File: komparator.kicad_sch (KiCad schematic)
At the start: 11 parts, among them Q1 2N3904, Q2 2N3904, Q3 2N3906

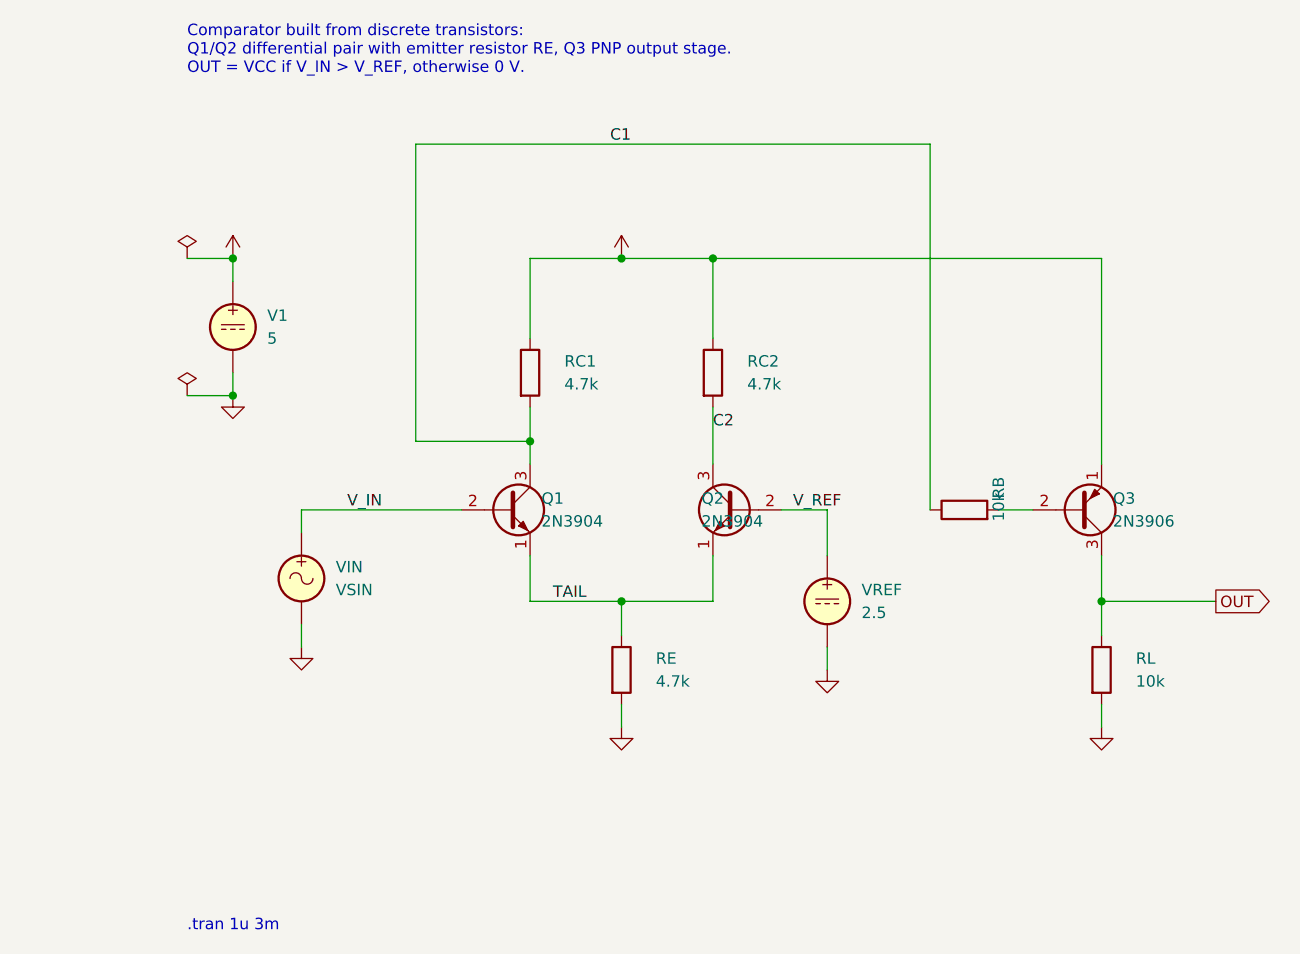
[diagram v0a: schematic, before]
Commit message: Run simulation with uv and take the KiCad schematic as parameter
- pyproject.toml + uv.lock replace requirements.txt
- simulate.py exports the given .kicad_sch via kicad-cli and simulates that
  netlist; VCC, V_REF and RE are read from the schematic
- schematic re-arranged by hand, references re-annotated by KiCad
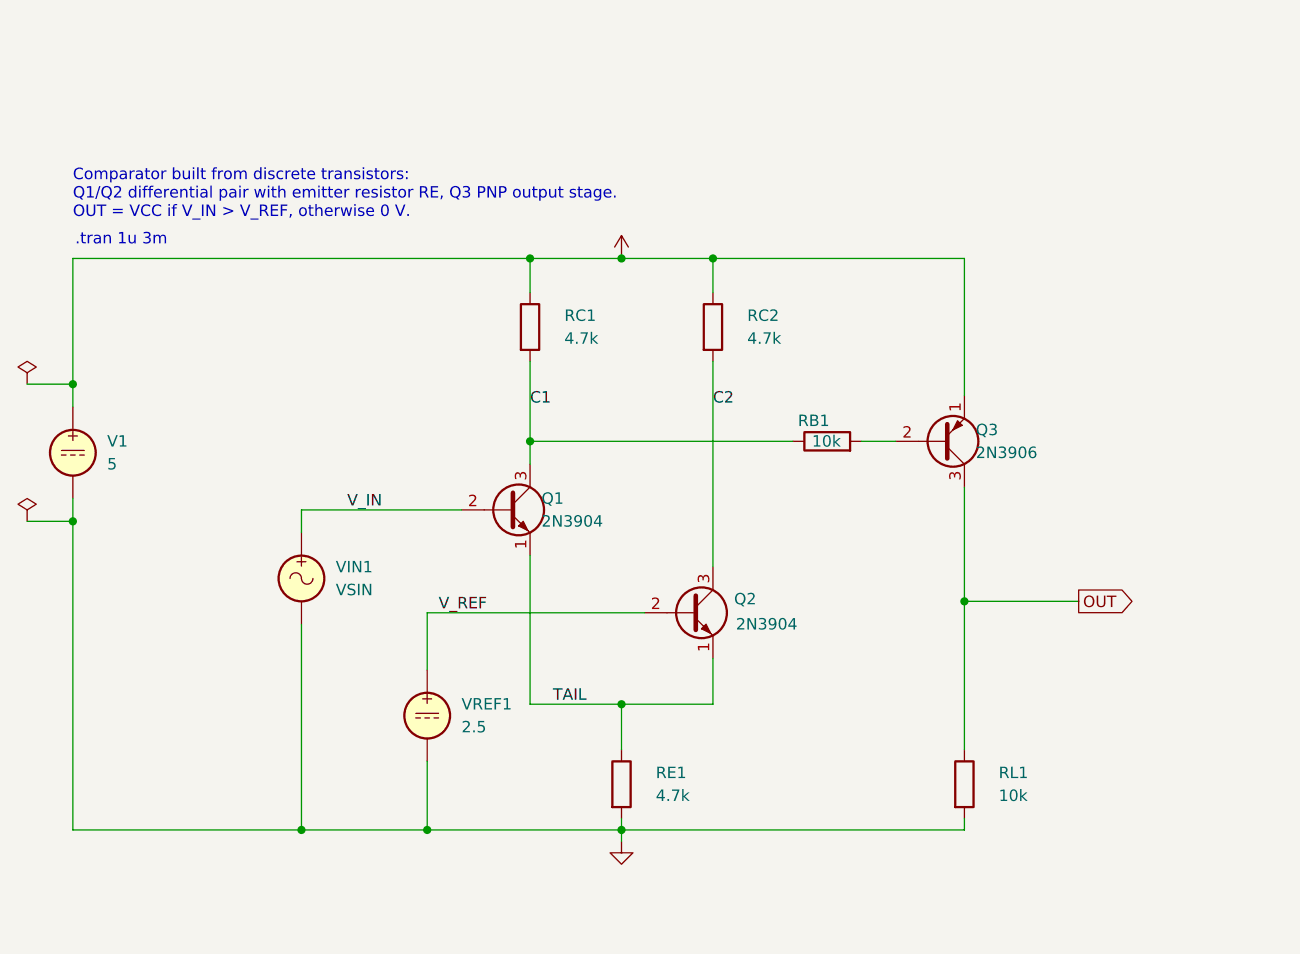
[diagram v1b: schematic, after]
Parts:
- removed VREF: 2.5, symbol Simulation_SPICE:VDC
- added VREF1: 2.5, symbol Simulation_SPICE:VDC
- renumbered RB to RB1, RE to RE1, RL to RL1, VIN to VIN1
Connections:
- net GND: now also VREF1.2
- net V_REF: now also VREF1.1
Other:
- moved on the sheet: Q2, Q3, RB1, RC1, RC2, RE1, RL1, V1
